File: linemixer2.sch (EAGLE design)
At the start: 75 parts, among them IC1 OPA2134P, IC2 OPA2134P, IC3 OPA2134P, IC4 OPA2134P, IC5 OPA2134P, IC6 BUF634P, J1 POWER_JACK

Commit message: change resistors to 3mm and tweak
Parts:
- R1, R10, R11, R12, R13, R14, R15, R16, R17, R18, R19, R2, R20, R21, R22, R23, R24, R25, R26, R27, R28, R29, R3, R30, R31, R4, R5, R6, R7, R8, R9: device SparkFun-Resistors:10KOHM-1/4W5%(PTH) -> adafruit:R-US_0204/5
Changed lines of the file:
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@@
 <part name="C7" library="SparkFun-Capacitors" deviceset="100UF-POLAR" device="-RADIAL-2.5MM-25V-20%" value="47u"/>
 <part name="C8" library="SparkFun-Capacitors" deviceset="100UF-POLAR" device="-RADIAL-2.5MM-25V-20%" value="47u"/>
-<part name="R1" library="SparkFun-Resistors" deviceset="10KOHM-1/4W5%(PTH)" device="" value="10k"/>
-<part name="R2" library="SparkFun-Resistors" deviceset="10KOHM-1/4W5%(PTH)" device="" value="10k"/>
-<part name="R3" library="SparkFun-Resistors" deviceset="10KOHM-1/4W5%(PTH)" device="" value="10k"/>
-<part name="R4" library="SparkFun-Resistors" deviceset="10KOHM-1/4W5%(PTH)" device="" value="10k"/>
-<part name="R5" library="SparkFun-Resistors" deviceset="10KOHM-1/4W5%(PTH)" device="" value="10k"/>
-<part name="R6" library="SparkFun-Resistors" deviceset="10KOHM-1/4W5%(PTH)" device="" value="10k"/>
-<part name="R7" library="SparkFun-Resistors" deviceset="10KOHM-1/4W5%(PTH)" device="" value="10k"/>
-<part name="R8" library="SparkFun-Resistors" deviceset="10KOHM-1/4W5%(PTH)" device="" value="10k"/>
-<part name="R9" library="SparkFun-Resistors" deviceset="10KOHM-1/4W5%(PTH)" device="" value="47k"/>
+<part name="R1" library="adafruit" deviceset="R-US_" device="0204/5" value="10k"/>
+<part name="R2" library="adafruit" deviceset="R-US_" device="0204/5" value="10k"/>
+<part name="R3" library="adafruit" deviceset="R-US_" device="0204/5" value="10k"/>
+<part name="R4" library="adafruit" deviceset="R-US_" device="0204/5" value="10k"/>
+<part name="R5" library="adafruit" deviceset="R-US_" device="0204/5" value="10k"/>
+<part name="R6" library="adafruit" deviceset="R-US_" device="0204/5" value="10k"/>
+<part name="R7" library="adafruit" deviceset="R-US_" device="0204/5" value="10k"/>
+<part name="R8" library="adafruit" deviceset="R-US_" device="0204/5" value="10k"/>
+<part name="R9" library="adafruit" deviceset="R-US_" device="0204/5" value="47k"/>
 <part name="GND6" library="SparkFun-Aesthetics" deviceset="GND" device=""/>
 <part name="SUPPLY1" library="SparkFun-Aesthetics" deviceset="VCC" device=""/>
 <part name="C9" library="SparkFun-Capacitors" deviceset="CAP" device="PTH" value="27pf"/>
 <part name="POT1_" library="myparts" deviceset="POT_BOURNS_PTD902" device="" value="10K"/>
-<part name="R10" library="SparkFun-Resistors" deviceset="10KOHM-1/4W5%(PTH)" device="" value="22k"/>
-<part name="R11" library="SparkFun-Resistors" deviceset="10KOHM-1/4W5%(PTH)" device="" value="47k"/>
+<part name="R10" library="adafruit" deviceset="R-US_" device="0204/5" value="22k"/>
+<part name="R11" library="adafruit" deviceset="R-US_" device="0204/5" value="47k"/>
 <part name="C10" library="SparkFun-Capacitors" deviceset="CAP" device="PTH" value="27pf"/>
-<part name="R12" library="SparkFun-Resistors" deviceset="10KOHM-1/4W5%(PTH)" device="" value="22k"/>
+<part name="R12" library="adafruit" deviceset="R-US_" device="0204/5" value="22k"/>
 <part name="IC2" library="burr-brown" deviceset="OPA2134" device="P"/>
-<part name="R13" library="SparkFun-Resistors" deviceset="10KOHM-1/4W5%(PTH)" device="" value="47k"/>
+<part name="R13" library="adafruit" deviceset="R-US_" device="0204/5" value="47k"/>
 <part name="GND7" library="SparkFun-Aesthetics" deviceset="GND" device=""/>
 <part name="SUPPLY2" library="SparkFun-Aesthetics" deviceset="VCC" device=""/>
 <part name="C11" library="SparkFun-Capacitors" deviceset="CAP" device="PTH" value="27pf"/>
 <part name="POT2_" library="myparts" deviceset="POT_BOURNS_PTD902" device="" value="10K"/>
-<part name="R14" library="SparkFun-Resistors" deviceset="10KOHM-1/4W5%(PTH)" device="" value="22k"/>
-<part name="R15" library="SparkFun-Resistors" deviceset="10KOHM-1/4W5%(PTH)" device="" value="47k"/>
+<part name="R14" library="adafruit" deviceset="R-US_" device="0204/5" value="22k"/>
+<part name="R15" library="adafruit" deviceset="R-US_" device="0204/5" value="47k"/>
 <part name="C12" library="SparkFun-Capacitors" deviceset="CAP" device="PTH" value="27pf"/>
-<part name="R16" library="SparkFun-Resistors" deviceset="10KOHM-1/4W5%(PTH)" device="" value="22k"/>
+<part name="R16" library="adafruit" deviceset="R-US_" device="0204/5" value="22k"/>
 <part name="IC3" library="burr-brown" deviceset="OPA2134" device="P"/>
-<part name="R17" library="SparkFun-Resistors" deviceset="10KOHM-1/4W5%(PTH)" device="" value="47k"/>
+<part name="R17" library="adafruit" deviceset="R-US_" device="0204/5" value="47k"/>
 <part name="GND8" library="SparkFun-Aesthetics" deviceset="GND" device=""/>
 <part name="SUPPLY3" library="SparkFun-Aesthetics" deviceset="VCC" device=""/>
 <part name="C13" library="SparkFun-Capacitors" deviceset="CAP" device="PTH" value="27pf"/>
 <part name="POT3_" library="myparts" deviceset="POT_BOURNS_PTD902" device="" value="10K"/>
-<part name="R18" library="SparkFun-Resistors" deviceset="10KOHM-1/4W5%(PTH)" device="" value="22k"/>
-<part name="R19" library="SparkFun-Resistors" deviceset="10KOHM-1/4W5%(PTH)" device="" value="47k"/>
+<part name="R18" library="adafruit" deviceset="R-US_" device="0204/5" value="22k"/>
+<part name="R19" library="adafruit" deviceset="R-US_" device="0204/5" value="47k"/>
 <part name="C14" library="SparkFun-Capacitors" deviceset="CAP" device="PTH" value="27pf"/>
-<part name="R20" library="SparkFun-Resistors" deviceset="10KOHM-1/4W5%(PTH)" device="" value="22k"/>
+<part name="R20" library="adafruit" deviceset="R-US_" device="0204/5" value="22k"/>
 <part name="IC4" library="burr-brown" deviceset="OPA2134" device="P"/>
-<part name="R21" library="SparkFun-Resistors" deviceset="10KOHM-1/4W5%(PTH)" device="" value="47k"/>
+<part name="R21" library="adafruit" deviceset="R-US_" device="0204/5" value="47k"/>
 <part name="GND9" library="SparkFun-Aesthetics" deviceset="GND" device=""/>
 <part name="SUPPLY4" library="SparkFun-Aesthetics" deviceset="VCC" device=""/>
 <part name="C15" library="SparkFun-Capacitors" deviceset="CAP" device="PTH" value="27pf"/>
 <part name="POT4_" library="myparts" deviceset="POT_BOURNS_PTD902" device="" value="10K"/>
-<part name="R22" library="SparkFun-Resistors" deviceset="10KOHM-1/4W5%(PTH)" device="" value="22k"/>
-<part name="R23" library="SparkFun-Resistors" deviceset="10KOHM-1/4W5%(PTH)" device="" value="47k"/>
+<part name="R22" library="adafruit" deviceset="R-US_" device="0204/5" value="22k"/>
+<part name="R23" library="adafruit" deviceset="R-US_" device="0204/5" value="47k"/>
 <part name="C16" library="SparkFun-Capacitors" deviceset="CAP" device="PTH" value="27pf"/>
-<part name="R24" library="SparkFun-Resistors" deviceset="10KOHM-1/4W5%(PTH)" device="" value="22k"/>
+<part name="R24" library="adafruit" deviceset="R-US_" device="0204/5" value="22k"/>
 <part name="C17" library="SparkFun-Capacitors" deviceset="100UF-POLAR" device="-RADIAL-2.5MM-25V-20%" value="100uF"/>
 <part name="C18" library="SparkFun-Capacitors" deviceset="100UF-POLAR" device="-RADIAL-2.5MM-25V-20%" value="100uF"/>
 <part name="SUPPLY5" library="SparkFun-Aesthetics" deviceset="VCC" device=""/>
 <part name="GND10" library="SparkFun-Aesthetics" deviceset="GND" device=""/>
-<part name="R25" library="SparkFun-Resistors" deviceset="10KOHM-1/4W5%(PTH)" device="" value="47"/>
-<part name="R26" library="SparkFun-Resistors" deviceset="10KOHM-1/4W5%(PTH)" device="" value="47"/>
-<part name="R27" library="SparkFun-Resistors" deviceset="10KOHM-1/4W5%(PTH)" device="" value="47k"/>
+<part name="R25" library="adafruit" deviceset="R-US_" device="0204/5" value="47"/>
+<part name="R26" library="adafruit" deviceset="R-US_" device="0204/5" value="47"/>
+<part name="R27" library="adafruit" deviceset="R-US_" device="0204/5" value="47k"/>
 <part name="C19" library="SparkFun-Capacitors" deviceset="CAP" device="PTH" value="27pf"/>
-<part name="R28" library="SparkFun-Resistors" deviceset="10KOHM-1/4W5%(PTH)" device="" value="47k"/>
+<part name="R28" library="adafruit" deviceset="R-US_" device="0204/5" value="47k"/>
 <part name="C20" library="SparkFun-Capacitors" deviceset="CAP" device="PTH" value="27pf"/>
 <part name="POT_MAIN_" library="myparts" deviceset="POT_BOURNS_PTR902" device="" value="10K"/>
@@
 <part name="J1" library="SparkFun-Connectors" deviceset="POWER_JACK" device=""/>
 <part name="C21" library="SparkFun-Capacitors" deviceset="100UF-POLAR" device="-RADIAL-2.5MM-25V-20%" value="100uF"/>
-<part name="R29" library="SparkFun-Resistors" deviceset="10KOHM-1/4W5%(PTH)" device="" value="10k"/>
-<part name="R30" library="SparkFun-Resistors" deviceset="10KOHM-1/4W5%(PTH)" device="" value="10k"/>
+<part name="R29" library="adafruit" deviceset="R-US_" device="0204/5" value="10k"/>
+<part name="R30" library="adafruit" deviceset="R-US_" device="0204/5" value="10k"/>
 <part name="U$1" library="myparts" deviceset="DP_LOGO" device=""/>
 <part name="PWR_LED" library="SparkFun-LED" deviceset="LED" device="3MM"/>
-<part name="R31" library="SparkFun-Resistors" deviceset="10KOHM-1/4W5%(PTH)" device="" value="1k"/>
+<part name="R31" library="adafruit" deviceset="R-US_" device="0204/5" value="1k"/>
 <part name="SUPPLY7" library="SparkFun-Aesthetics" deviceset="VCC" device=""/>
 <part name="GND12" library="SparkFun-Aesthetics" deviceset="GND" device=""/>

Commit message: rev b
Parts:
- removed C24: 47u, SparkFun-Capacitors:100UF-POLAR-RADIAL-2.5MM-25V-20%
- removed IC6: BUF634P, burr-brown:BUF634P
- removed R29, R30: 10k, adafruit:R-US_0204/5
- added U$2: TLE2426-TO_92, myparts:TLE2426-TO_92
- R1, R2, R3, R4, R5, R6, R7, R8: value 10k -> 1k
- R10, R12, R14, R16, R18, R20, R22, R24: value 22k -> 1k
- R11, R13, R15, R17, R19, R21, R23, R27, R28, R9: value 47k -> 1k
- R31: value 1k -> 5k
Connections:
- removed net N$19: POT1_1.W, R10.1
- removed net N$20: POT2_1.W, R14.1
- removed net N$24: POT1_2.W, R12.1
- removed net N$26: POT2_2.W, R16.1
- removed net N$28: POT3_1.W, R18.1
- removed net N$30: POT3_2.W, R20.1
- removed net N$32: POT4_1.W, R22.1
- removed net N$34: POT4_2.W, R24.1
- removed net N$44: C24.+, IC6.IN, R29.1, R30.2
- new net N$40: C9.1, IC1A.-IN, POT1_2.W, R9.1
- new net N$50: C13.1, IC3A.-IN, POT3_2.W, R17.1
- new net N$51: C11.1, IC2A.-IN, POT2_2.W, R13.1
- new net N$52: C15.1, IC4A.-IN, POT4_2.W, R21.1
- new net N$60: C10.1, IC1B.-IN, POT1_1.W, R11.1
- new net N$61: C12.1, IC2B.-IN, POT2_1.W, R15.1
- new net N$62: C14.1, IC3B.-IN, POT3_1.W, R19.1
- new net N$64: C16.1, IC4B.-IN, POT4_1.W, R23.1
- net BUS_L: now also R10.2, R14.2, R18.2, R22.2; no longer R12.2, R16.2, R20.2, R24.2
- net BUS_R: now also R12.2, R16.2, R20.2, R24.2; no longer R10.2, R14.2, R18.2, R22.2
- net GND: now also POT1_1.A, POT1_2.A, POT2_1.A, POT2_2.A, POT3_1.A, POT3_2.A, POT4_1.A, POT4_2.A, POT_MAIN_1.A, POT_MAIN_2.A, U$2.COM; no longer C24.-, IC6.BW, IC6.V-, R30.1
- net IN1_L: now also POT1_2.B, R1.2; no longer C10.1, IC1B.-IN, R11.1, R2.2
- net IN1_R: now also POT1_1.B, R2.2; no longer C9.1, IC1A.-IN, R1.2, R9.1
- net IN2_L: now also POT2_2.B, R3.2; no longer C12.1, IC2B.-IN, R15.1, R4.2
- net IN2_R: now also POT2_1.B, R4.2; no longer C11.1, IC2A.-IN, R13.1, R3.2
- net IN3_L: now also POT3_2.B, R5.2; no longer C14.1, IC3B.-IN, R19.1, R6.2
- net IN3_R: now also POT3_1.B, R6.2; no longer C13.1, IC3A.-IN, R17.1, R5.2
- net IN4_L: now also POT4_2.B, R7.2; no longer C16.1, IC4B.-IN, R23.1, R8.2
- net IN4_R: now also POT4_1.B, R8.2; no longer C15.1, IC4A.-IN, R21.1, R7.2
- net N$17: now also R10.1; no longer POT1_1.B
- net N$18: now also R14.1; no longer POT2_1.B
- net N$21: now also R12.1; no longer POT1_2.B
- net N$25: now also R16.1; no longer POT2_2.B
- net N$27: now also R18.1; no longer POT3_1.B
- net N$29: now also R20.1; no longer POT3_2.B
- net N$31: now also R22.1; no longer POT4_1.B
- net N$33: now also R24.1; no longer POT4_2.B
- net OUT_L: now also POT_MAIN_1.W; no longer POT_MAIN_2.W
- net OUT_R: now also POT_MAIN_2.W; no longer POT_MAIN_1.W
- net VCC: now also U$2.IN; no longer IC6.V+, R29.2
- net VGND: now also U$2.OUT; no longer IC6.OUT, POT1_1.A, POT1_2.A, POT2_1.A, POT2_2.A, POT3_1.A, POT3_2.A, POT4_1.A, POT4_2.A, POT_MAIN_1.A, POT_MAIN_2.A
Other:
- note added: "2017-06-12"
- note added: "Rev B"
- note removed: "2017-05-27"
- note removed: "Rev A"
- moved on the sheet: C10, C11, C12, C13, C14, C15, C16, C9, IC1A, IC1B, IC2A, IC2B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

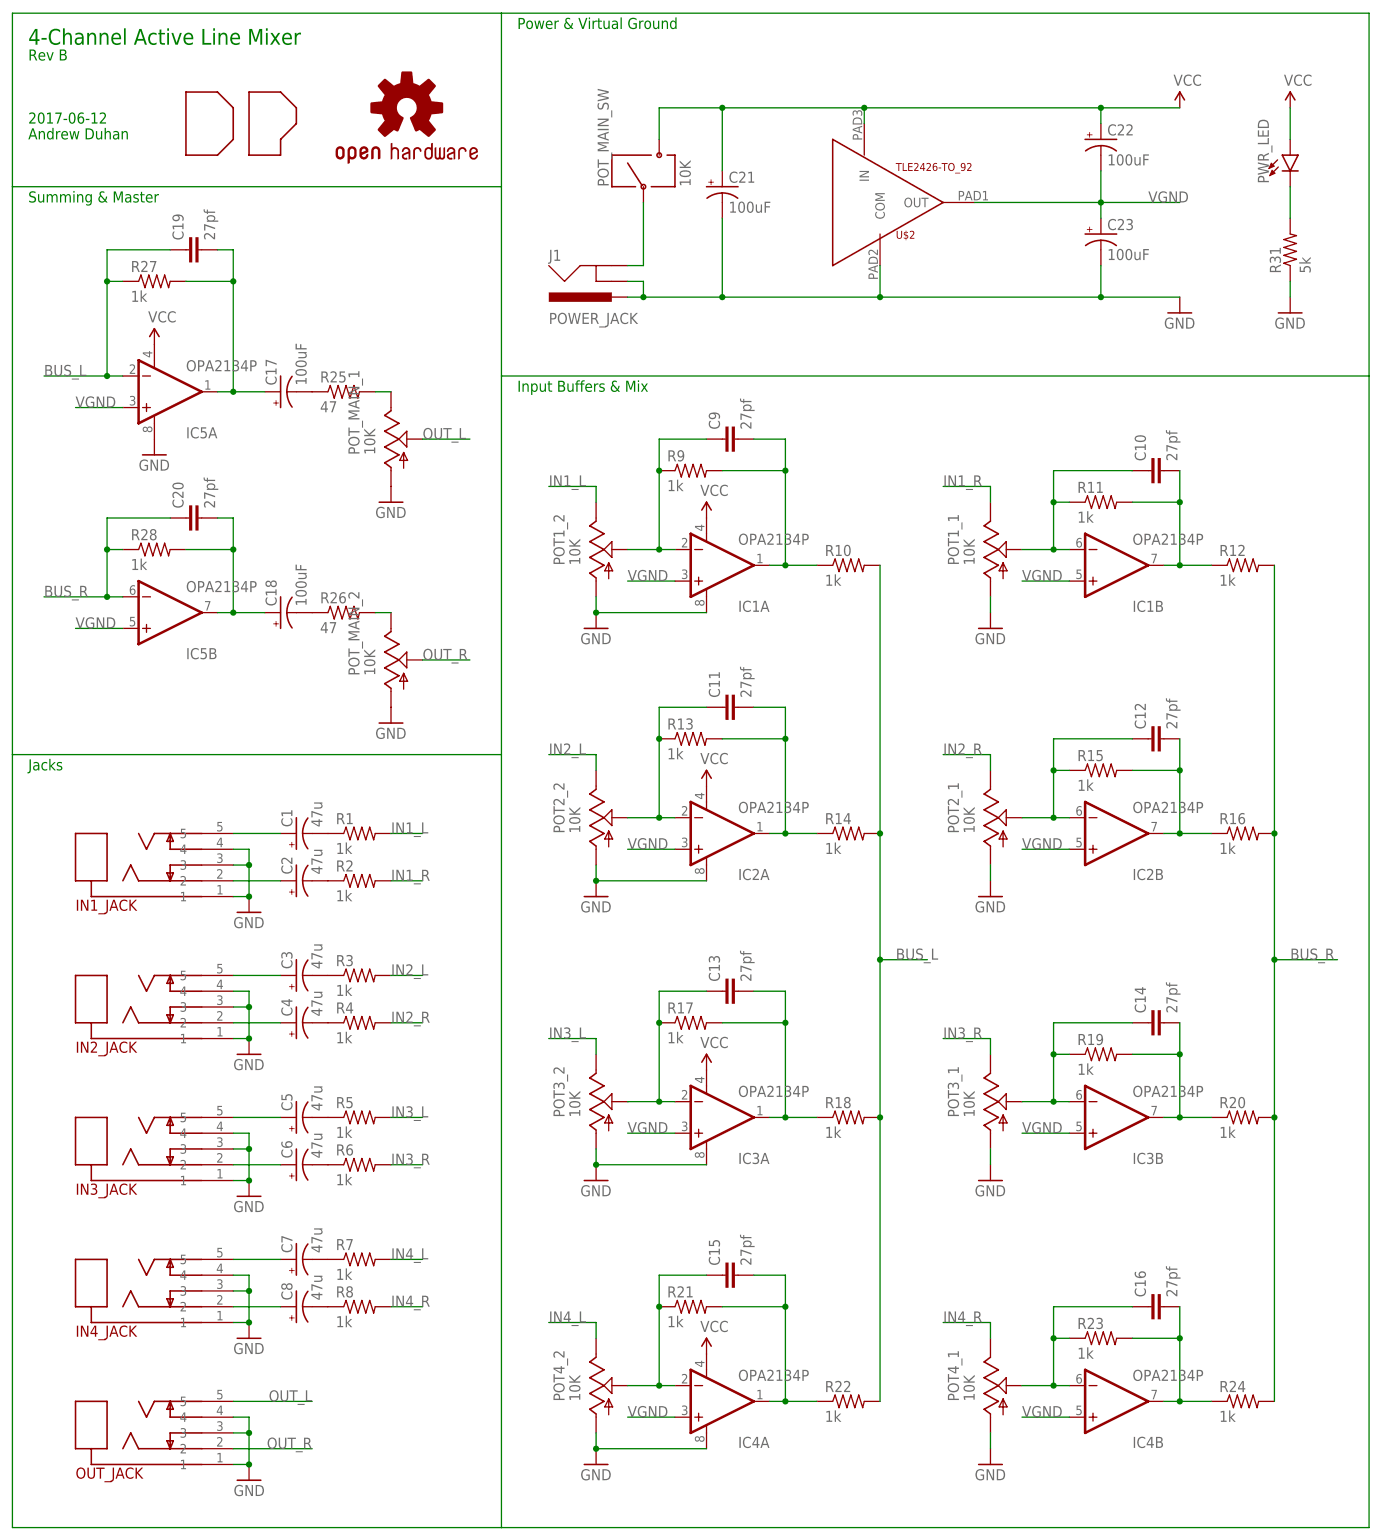
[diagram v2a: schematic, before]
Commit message: rev c - add resistors to the vgnd on each opamp
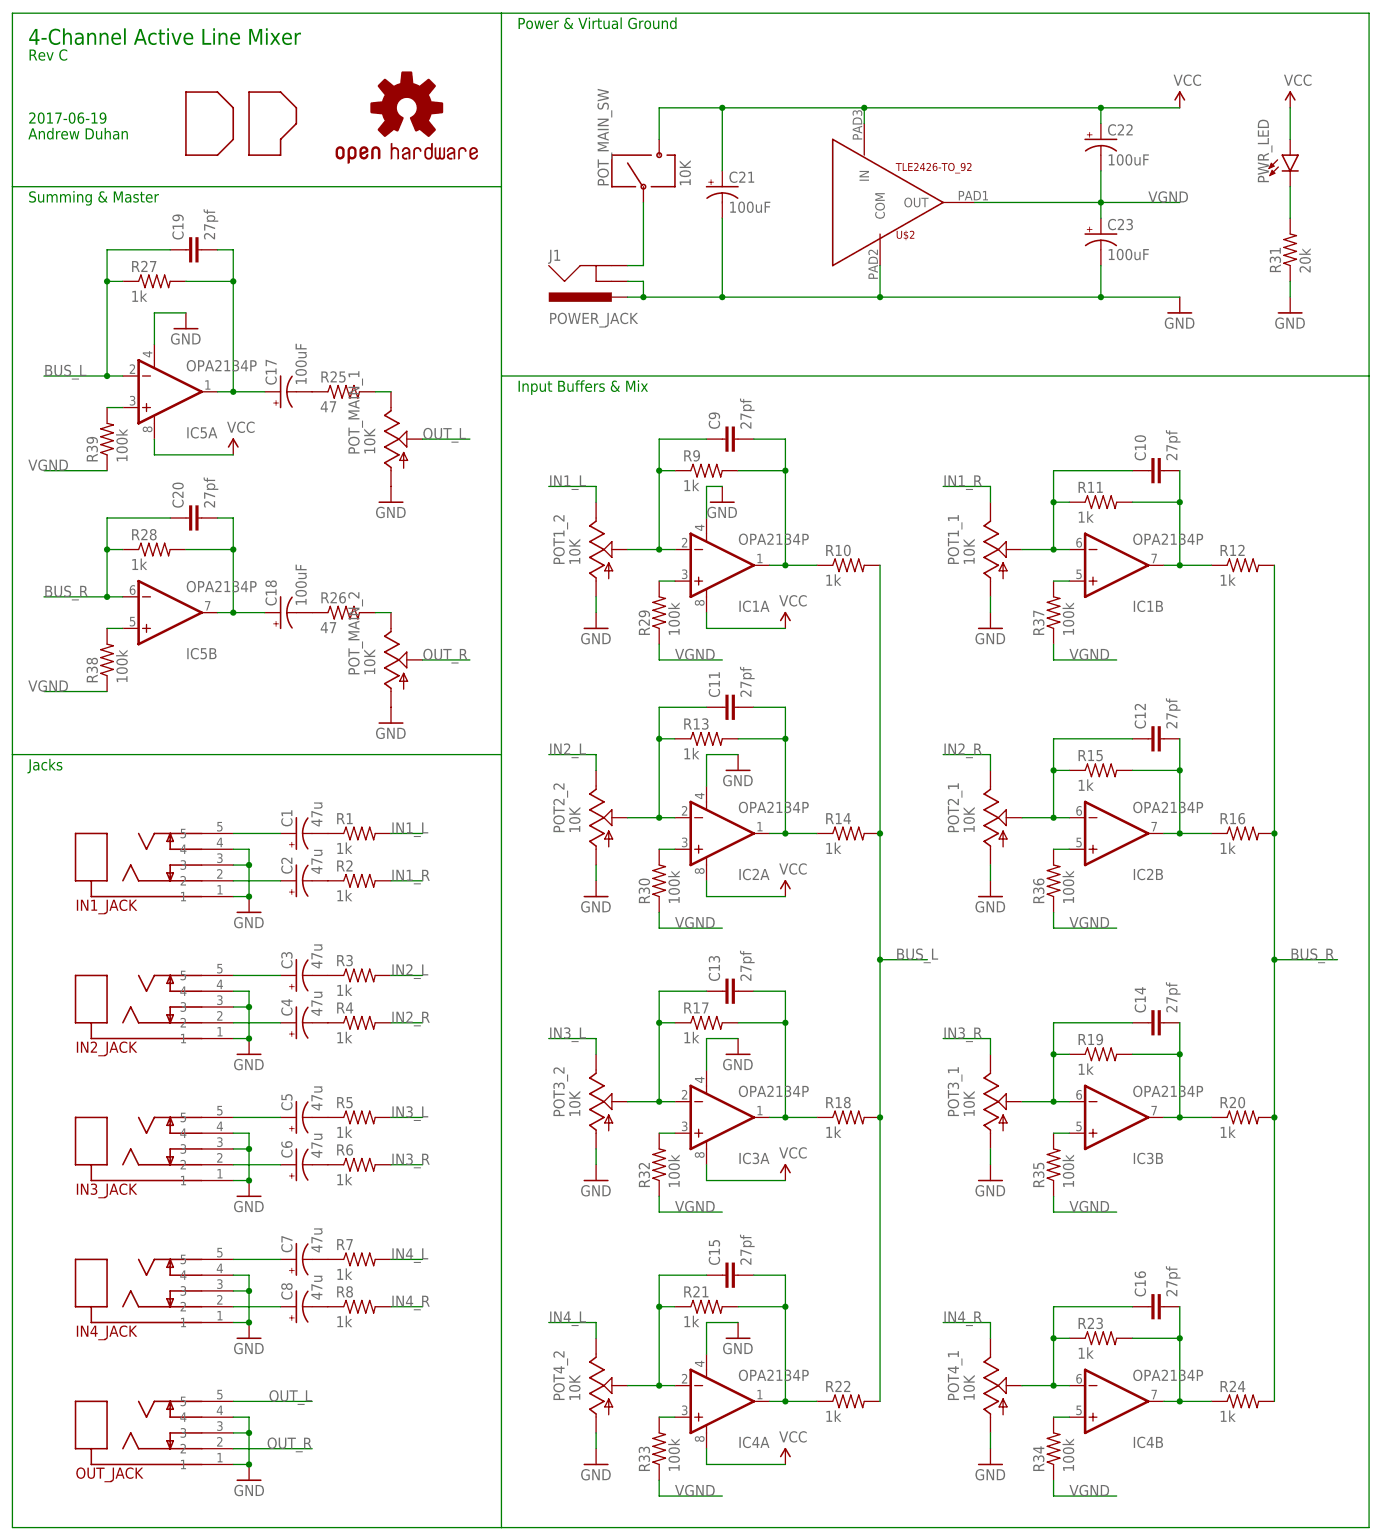
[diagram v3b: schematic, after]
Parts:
- added R29, R30, R32, R33, R34, R35, R36, R37, R38, R39: 100k, adafruit:R-US_0204/5
- R31: value 5k -> 20k
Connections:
- new net N$19: IC1A.+IN, R29.2
- new net N$20: IC5A.+IN, R39.2
- new net N$24: IC5B.+IN, R38.2
- new net N$30: IC2A.+IN, R30.2
- new net N$34: IC3A.+IN, R32.2
- new net N$44: IC4A.+IN, R33.2
- new net N$46: IC4B.+IN, R34.2
- new net N$48: IC3B.+IN, R35.2
- new net N$53: IC2B.+IN, R36.2
- new net N$55: IC1B.+IN, R37.2
- net GND: now also IC1A.V-, IC2A.V-, IC3A.V-, IC4A.V-, IC5A.V-; no longer IC1A.V+, IC2A.V+, IC3A.V+, IC4A.V+, IC5A.V+
- net VCC: now also IC1A.V+, IC2A.V+, IC3A.V+, IC4A.V+, IC5A.V+; no longer IC1A.V-, IC2A.V-, IC3A.V-, IC4A.V-, IC5A.V-
- net VGND: now also R29.1, R30.1, R32.1, R33.1, R34.1, R35.1, R36.1, R37.1, R38.1, R39.1; no longer IC1A.+IN, IC1B.+IN, IC2A.+IN, IC2B.+IN, IC3A.+IN, IC3B.+IN, IC4A.+IN, IC4B.+IN, IC5A.+IN, IC5B.+IN
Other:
- note added: "2017-06-19"
- note added: "Rev C"
- note removed: "2017-06-12"
- note removed: "Rev B"
- moved on the sheet: R13, R17, R21, R9
